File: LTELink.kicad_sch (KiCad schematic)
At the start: 0 parts

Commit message: mostly done except for RTL8305 power stuff
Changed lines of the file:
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@@
 	)
 	(sheet
-		(at 177.8 87.63)
+		(at 176.53 83.82)
 		(size 39.37 33.02)
 		(exclude_from_sim no)
@@
 		)
 		(property "Sheetname" "uart"
-			(at 177.8 86.9184 0)
+			(at 176.53 83.1084 0)
 			(effects
 				(font
@@
 		)
 		(property "Sheetfile" "uart.kicad_sch"
-			(at 177.8 121.2346 0)
+			(at 176.53 117.4246 0)
 			(effects
 				(font
@@
 	)
 	(sheet
-		(at 71.12 99.06)
-		(size 27.94 25.4)
+		(at 71.12 105.41)
+		(size 27.94 19.05)
 		(exclude_from_sim no)
 		(in_bom yes)
@@
 		)
 		(property "Sheetname" "USB"
-			(at 71.12 98.3484 0)
-			(effects
-				(font
+			(at 71.12 104.6984 0)
+			(effects
+				(font

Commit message: Finally done the layout
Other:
- sheet uart ports: added MAVLINK_RX, MAVLINK_TX, UART3_RX, UART3_TX, UART7_RX, UART7_TX; removed none
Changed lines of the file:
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@@
+	(wire
+		(pts
+			(xy 170.18 86.36) (xy 176.53 86.36)
+		)
+		(stroke
+			(width 0)
+			(type default)
+		)
+	)
 	(wire
 		(pts
@@
 	(wire
 		(pts
+			(xy 170.18 88.9) (xy 176.53 88.9)
+		)
+		(stroke
+			(width 0)
+			(type default)
+		)
+	)
+	(wire
+		(pts
 			(xy 97.79 146.05) (xy 116.84 146.05)
 		)
@@
 	(wire
 		(pts
+			(xy 170.18 105.41) (xy 176.53 105.41)
+		)
+		(stroke
+			(width 0)
+			(type default)
+		)
+	)
+	(wire
+		(pts
 			(xy 170.18 140.97) (xy 181.61 140.97)
 		)
@@
 	(wire
 		(pts
+			(xy 170.18 92.71) (xy 176.53 92.71)
+		)
+		(stroke
+			(width 0)
+			(type default)
+		)
+	)
+	(wire
+		(pts
+			(xy 170.18 95.25) (xy 176.53 95.25)
+		)
+		(stroke
+			(width 0)
+			(type default)
+		)
+	)
+	(wire
+		(pts
 			(xy 99.06 62.23) (xy 116.84 62.23)
+		)
+		(stroke
+			(width 0)
+			(type default)
+		)
+	)
+	(wire
+		(pts
+			(xy 170.18 107.95) (xy 176.53 107.95)
 		)
 		(stroke
@@
 			)
 		)
+		(pin "MAVLINK_RX" input
+			(at 176.53 86.36 180)
+			(effects
+				(font
+					(size 1.27 1.27)
+				)
+				(justify left)
+			)
+		)
+		(pin "MAVLINK_TX" output
+			(at 176.53 88.9 180)
+			(effects
+				(font
+					(size 1.27 1.27)
+				)
+				(justify left)
+			)
+		)
+		(pin "UART3_RX" input
+			(at 176.53 92.71 180)
+			(effects
+				(font
+					(size 1.27 1.27)
+				)
+				(justify left)
+			)
+		)
+		(pin "UART3_TX" output
+			(at 176.53 95.25 180)
+			(effects
+				(font
+					(size 1.27 1.27)
+				)
+				(justify left)
+			)
+		)
+		(pin "UART7_RX" input
+			(at 176.53 105.41 180)
+			(effects
+				(font
+					(size 1.27 1.27)
+				)
+				(justify left)
+			)
+		)
+		(pin "UART7_TX" output
+			(at 176.53 107.95 180)
+			(effects
+				(font
+					(size 1.27 1.27)
+				)
+				(justify left)
+			)
+		)

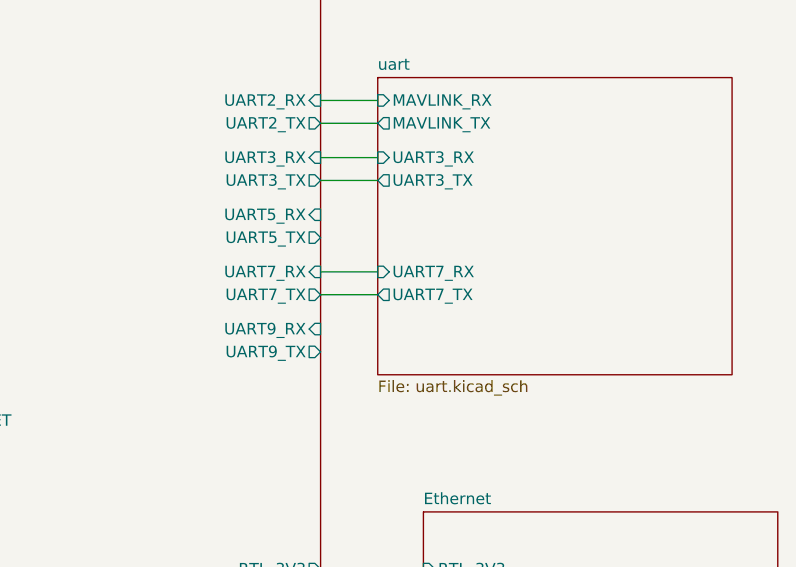
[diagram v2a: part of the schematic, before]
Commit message: fix incorrect footprint orientation and breakout uarts
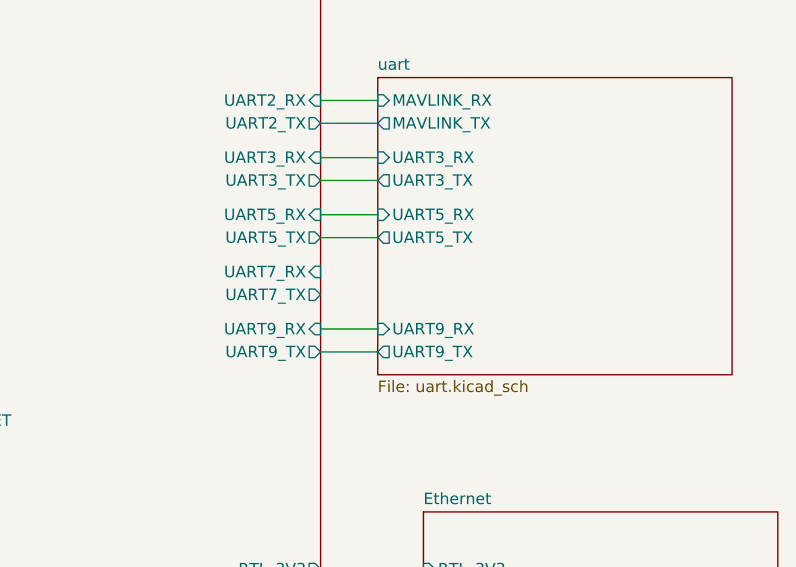
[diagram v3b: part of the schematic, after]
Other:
- sheet uart ports: added UART5_RX, UART5_TX, UART9_RX, UART9_TX; removed UART7_RX, UART7_TX
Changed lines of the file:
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@@
+	(wire
+		(pts
+			(xy 170.18 101.6) (xy 176.53 101.6)
+		)
+		(stroke
+			(width 0)
+			(type default)
+		)
+	)
 	(wire
 		(pts
@@
 	(wire
 		(pts
+			(xy 170.18 99.06) (xy 176.53 99.06)
+		)
+		(stroke
+			(width 0)
+			(type default)
+		)
+	)
+	(wire
+		(pts
 			(xy 99.06 64.77) (xy 116.84 64.77)
 		)
@@
 	(wire
 		(pts
-			(xy 170.18 105.41) (xy 176.53 105.41)
+			(xy 170.18 114.3) (xy 176.53 114.3)
 		)
 		(stroke
@@
 	(wire
 		(pts
-			(xy 170.18 107.95) (xy 176.53 107.95)
+			(xy 170.18 111.76) (xy 176.53 111.76)
 		)
 		(stroke
@@
 			)
 		)
-		(pin "UART7_RX" input
-			(at 176.53 105.41 180)
-			(effects
-				(font
-					(size 1.27 1.27)
-				)
-				(justify left)
-			)
-		)
-		(pin "UART7_TX" output
-			(at 176.53 107.95 180)
-			(effects
-				(font
+		(pin "UART9_RX" input
+			(at 176.53 111.76 180)
+			(effects
+				(font
+					(size 1.27 1.27)
+				)
+				(justify left)
+			)
+		)
+		(pin "UART9_TX" output
+			(at 176.53 114.3 180)
+			(effects
+				(font
+					(size 1.27 1.27)
+				)
+				(justify left)
+			)
+		)
+		(pin "UART5_RX" input
+			(at 176.53 99.06 180)
+			(effects
+				(font
+					(size 1.27 1.27)
+				)
+				(justify left)
+			)
+		)
+		(pin "UART5_TX" output
+			(at 176.53 101.6 180)
+			(effects
+				(font
